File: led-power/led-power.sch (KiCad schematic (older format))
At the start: 70 parts, among them J1 String1, J10 PowerInput, J2 String2, J3 String3, J4 String4, J5 String5, J6 String6, J7 String7, J8 String8, J9 PowerInput, Q1 Q_NMOS_GDS, Q2 Q_NMOS_GDS, Q3 Q_NMOS_GDS, Q4 Q_NMOS_GDS, Q5 Q_NMOS_GDS, Q6 Q_NMOS_GDS, Q7 Q_NMOS_GDS, Q8 Q_NMOS_GDS, U1 MCP6V51, U10 L78L05ACZ-AP, U11 MCP1501, U2 MCP6V51, U3 MCP6V51, U4 MCP6V51, U5 MCP6V51, U6 MCP6V51, U7 MCP6V51, U8 MCP6V51

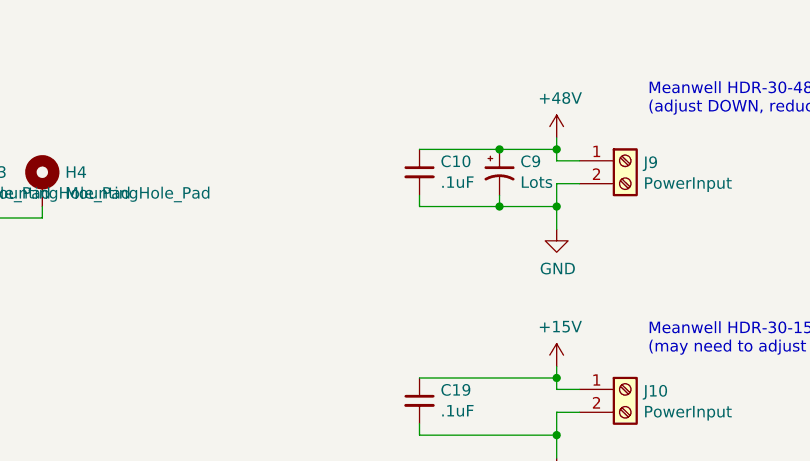
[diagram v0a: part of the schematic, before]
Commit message: Lots of LED power bring-up corrections
* MSOP-8 footprint for op amps
* TO-220 footprint for FETs
* Moved C10 away from J9
* Stopped bothering with length-adjusted traces to resistors
* Moved diodes away from LED strip terminals
* Silkscreen tweaks
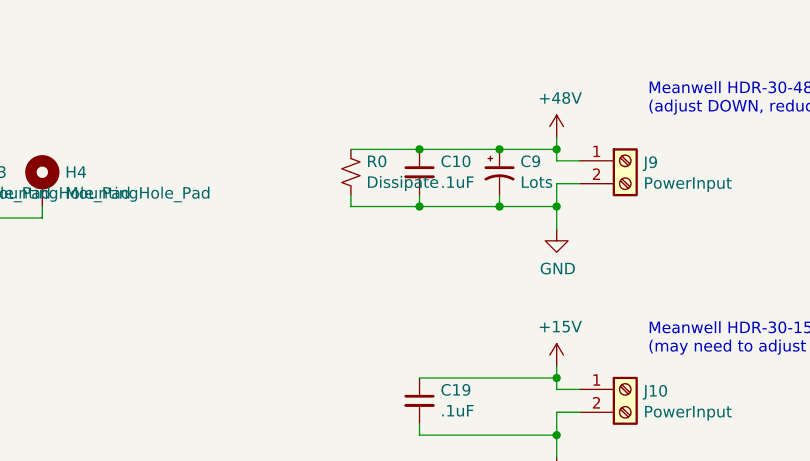
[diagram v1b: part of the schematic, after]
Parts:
- added R0: Dissipate, Resistors_SMD:R_0805_HandSoldering, symbol Device:R_Small_US
- Q1, Q2, Q3, Q4, Q5, Q6, Q7, Q8: footprint TO_SOT_Packages_THT:SIPAK_Vertical -> TO_SOT_Packages_THT:TO-220-3_Vertical
- U1, U2, U3, U4, U5, U6, U7, U8: footprint SMD_Packages:SOIC-8-N -> Housings_SSOP:MSOP-8_3x3mm_Pitch0.65mm
- U10: footprint TO_SOT_Packages_THT:TO-92_Inline_Narrow_Oval -> TO_SOT_Packages_THT:TO-92_Inline_Wide
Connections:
- net +48V: now also R0.1
- net GND: now also R0.2
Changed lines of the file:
@@
 F 0 "Q1" H 2404 1596 50  0000 L CNN
 F 1 "Q_NMOS_GDS" H 2404 1505 50  0000 L CNN
-F 2 "TO_SOT_Packages_THT:SIPAK_Vertical" H 2400 1650 50  0001 C CNN
+F 2 "TO_SOT_Packages_THT:TO-220-3_Vertical" H 2400 1650 50  0001 C CNN
 F 3 "~" H 2200 1550 50  0001 C CNN
 	1    2200 1550
@@
 F 0 "U1" H 1550 1900 50  0000 L CNN
 F 1 "MCP6V51" H 1550 1800 50  0000 L CNN
-F 2 "SMD_Packages:SOIC-8-N" H 1450 1350 50  0001 L CNN
+F 2 "Housings_SSOP:MSOP-8_3x3mm_Pitch0.65mm" H 1450 1350 50  0001 L CNN
 F 3 "http://www.ti.com/lit/ds/symlink/lm6171.pdf" H 1700 1700 50  0001 C CNN
 	1    1550 1550
@@
 F 0 "U10" H 14450 2242 50  0000 C CNN
 F 1 "L78L05ACZ-AP" H 14450 2151 50  0000 C CNN
-F 2 "TO_SOT_Packages_THT:TO-92_Inline_Narrow_Oval" H 14450 2225 50  0001 C CIN
+F 2 "TO_SOT_Packages_THT:TO-92_Inline_Wide" H 14450 2225 50  0001 C CIN
 F 3 "https://www.onsemi.cn/PowerSolutions/document/MC7800-D.PDF" H 14450 1950 50  0001 C CNN
 	1    14450 2000
@@
 F 0 "Q2" H 2404 3346 50  0000 L CNN
 F 1 "Q_NMOS_GDS" H 2404 3255 50  0000 L CNN
-F 2 "TO_SOT_Packages_THT:SIPAK_Vertical" H 2400 3400 50  0001 C CNN
+F 2 "TO_SOT_Packages_THT:TO-220-3_Vertical" H 2400 3400 50  0001 C CNN
 F 3 "~" H 2200 3300 50  0001 C CNN
 	1    2200 3300
@@
 F 0 "U2" H 1550 3650 50  0000 L CNN
 F 1 "MCP6V51" H 1550 3550 50  0000 L CNN
-F 2 "SMD_Packages:SOIC-8-N" H 1450 3100 50  0001 L CNN
+F 2 "Housings_SSOP:MSOP-8_3x3mm_Pitch0.65mm" H 1450 3100 50  0001 L CNN
 F 3 "http://www.ti.com/lit/ds/symlink/lm6171.pdf" H 1700 3450 50  0001 C CNN
 	1    1550 3300
@@
 F 0 "Q3" H 2404 5096 50  0000 L CNN
 F 1 "Q_NMOS_GDS" H 2404 5005 50  0000 L CNN
-F 2 "TO_SOT_Packages_THT:SIPAK_Vertical" H 2400 5150 50  0001 C CNN
+F 2 "TO_SOT_Packages_THT:TO-220-3_Vertical" H 2400 5150 50  0001 C CNN
 F 3 "~" H 2200 5050 50  0001 C CNN
 	1    2200 5050
@@
 F 0 "U3" H 1550 5400 50  0000 L CNN
 F 1 "MCP6V51" H 1550 5300 50  0000 L CNN
-F 2 "SMD_Packages:SOIC-8-N" H 1450 4850 50  0001 L CNN
+F 2 "Housings_SSOP:MSOP-8_3x3mm_Pitch0.65mm" H 1450 4850 50  0001 L CNN
 F 3 "http://www.ti.com/lit/ds/symlink/lm6171.pdf" H 1700 5200 50  0001 C CNN
 	1    1550 5050
@@
 F 0 "Q4" H 2404 6846 50  0000 L CNN
 F 1 "Q_NMOS_GDS" H 2404 6755 50  0000 L CNN
-F 2 "TO_SOT_Packages_THT:SIPAK_Vertical" H 2400 6900 50  0001 C CNN
+F 2 "TO_SOT_Packages_THT:TO-220-3_Vertical" H 2400 6900 50  0001 C CNN
 F 3 "~" H 2200 6800 50  0001 C CNN
 	1    2200 6800
@@
 F 0 "U4" H 1550 7150 50  0000 L CNN
 F 1 "MCP6V51" H 1550 7050 50  0000 L CNN
-F 2 "SMD_Packages:SOIC-8-N" H 1450 6600 50  0001 L CNN
+F 2 "Housings_SSOP:MSOP-8_3x3mm_Pitch0.65mm" H 1450 6600 50  0001 L CNN
 F 3 "http://www.ti.com/lit/ds/symlink/lm6171.pdf" H 1700 6950 50  0001 C CNN
 	1    1550 6800
@@
 F 0 "Q5" H 5204 1596 50  0000 L CNN
 F 1 "Q_NMOS_GDS" H 5204 1505 50  0000 L CNN
-F 2 "TO_SOT_Packages_THT:SIPAK_Vertical" H 5200 1650 50  0001 C CNN
+F 2 "TO_SOT_Packages_THT:TO-220-3_Vertical" H 5200 1650 50  0001 C CNN
 F 3 "~" H 5000 1550 50  0001 C CNN
 	1    5000 1550
@@
 F 0 "U5" H 4350 1900 50  0000 L CNN
 F 1 "MCP6V51" H 4350 1800 50  0000 L CNN
-F 2 "SMD_Packages:SOIC-8-N" H 4250 1350 50  0001 L CNN
+F 2 "Housings_SSOP:MSOP-8_3x3mm_Pitch0.65mm" H 4250 1350 50  0001 L CNN
 F 3 "http://www.ti.com/lit/ds/symlink/lm6171.pdf" H 4500 1700 50  0001 C CNN
 	1    4350 1550
@@
 F 0 "Q6" H 5204 3296 50  0000 L CNN
 F 1 "Q_NMOS_GDS" H 5204 3205 50  0000 L CNN
-F 2 "TO_SOT_Packages_THT:SIPAK_Vertical" H 5200 3350 50  0001 C CNN
+F 2 "TO_SOT_Packages_THT:TO-220-3_Vertical" H 5200 3350 50  0001 C CNN
 F 3 "~" H 5000 3250 50  0001 C CNN
 	1    5000 3250
@@
 F 0 "U6" H 4350 3600 50  0000 L CNN
 F 1 "MCP6V51" H 4350 3500 50  0000 L CNN
-F 2 "SMD_Packages:SOIC-8-N" H 4250 3050 50  0001 L CNN
+F 2 "Housings_SSOP:MSOP-8_3x3mm_Pitch0.65mm" H 4250 3050 50  0001 L CNN
 F 3 "http://www.ti.com/lit/ds/symlink/lm6171.pdf" H 4500 3400 50  0001 C CNN
 	1    4350 3250
@@
 F 0 "Q7" H 5204 5096 50  0000 L CNN
 F 1 "Q_NMOS_GDS" H 5204 5005 50  0000 L CNN
-F 2 "TO_SOT_Packages_THT:SIPAK_Vertical" H 5200 5150 50  0001 C CNN
+F 2 "TO_SOT_Packages_THT:TO-220-3_Vertical" H 5200 5150 50  0001 C CNN
 F 3 "~" H 5000 5050 50  0001 C CNN
 	1    5000 5050
@@
 F 0 "U7" H 4350 5400 50  0000 L CNN
 F 1 "MCP6V51" H 4350 5300 50  0000 L CNN
-F 2 "SMD_Packages:SOIC-8-N" H 4250 4850 50  0001 L CNN
+F 2 "Housings_SSOP:MSOP-8_3x3mm_Pitch0.65mm" H 4250 4850 50  0001 L CNN
 F 3 "http://www.ti.com/lit/ds/symlink/lm6171.pdf" H 4500 5200 50  0001 C CNN
 	1    4350 5050
@@
 F 0 "Q8" H 5204 6796 50  0000 L CNN
 F 1 "Q_NMOS_GDS" H 5204 6705 50  0000 L CNN
-F 2 "TO_SOT_Packages_THT:SIPAK_Vertical" H 5200 6850 50  0001 C CNN
+F 2 "TO_SOT_Packages_THT:TO-220-3_Vertical" H 5200 6850 50  0001 C CNN
 F 3 "~" H 5000 6750 50  0001 C CNN
 	1    5000 6750
@@
 F 0 "U8" H 4350 7100 50  0000 L CNN
 F 1 "MCP6V51" H 4350 7000 50  0000 L CNN
-F 2 "SMD_Packages:SOIC-8-N" H 4250 6550 50  0001 L CNN
+F 2 "Housings_SSOP:MSOP-8_3x3mm_Pitch0.65mm" H 4250 6550 50  0001 L CNN
 F 3 "http://www.ti.com/lit/ds/symlink/lm6171.pdf" H 4500 6900 50  0001 C CNN
 	1    4350 6750
@@
 Wire Wire Line
 	14850 2000 15000 2000
+$Comp
+L Device:R_Small_US R0
+U 1 1 5FE12C48
+P 9800 1300
+F 0 "R0" H 9868 1346 50  0000 L CNN
+F 1 "Dissipate" H 9868 1255 50  0000 L CNN
+F 2 "Resistors_SMD:R_0805_HandSoldering" H 9800 1300 50  0001 C CNN
+F 3 "~" H 9800 1300 50  0001 C CNN
+	1    9800 1300
+	1    0    0    -1
+$EndComp
+Wire Wire Line
+	10100 1200 9800 1200
+Connection ~ 10100 1200
+Wire Wire Line
+	9800 1400 9800 1450
+Wire Wire Line
+	9800 1450 10100 1450
+Connection ~ 10100 1450
 $EndSCHEMATC

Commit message: Reverse polarity diodes; Qwiic header&IO Expander
Also includes relevant connections for the IO expander to the
feedback nets, and /SHDN on the voltage reference.
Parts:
- added C21: 4.7uF, Capacitors_SMD:C_0805_HandSoldering, symbol Device:C_Small
- added C22: 0.1uF, Capacitors_SMD:C_0805_HandSoldering, symbol Device:C_Small
- added C23: 300pF, Capacitors_SMD:C_0805_HandSoldering, symbol Device:C_Small
- added D10, D9: D_Small_ALT, Diodes_SMD:D_SOD-123F, symbol Device:D_Small_ALT
- added J11: Qwiic, Connectors_JST:JST_SH_SM04B-SRSS-TB_04x1.00mm_Angled, symbol Connector:Conn_01x04_Female
- added R11, R12, R13, R14, R15, R16, R17, R18: 43k, Resistors_SMD:R_0805_HandSoldering, symbol Device:R_Small_US
- added R9: 3600, Resistors_SMD:R_0805_HandSoldering, symbol Device:R_Small_US
- added U9: MCP23017_SO, Housings_SOIC:SOIC-28W_7.5x17.9mm_Pitch1.27mm, symbol Interface_Expansion:MCP23017_SO
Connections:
- net +15V: now also D10.1 (K); no longer J10.1 (Pin_1)
- net +48V: now also D9.1 (K); no longer J9.1 (Pin_1)
- net +5V: now also R9.1; no longer U11.3 (/SHDN)
- net GND: now also C21.2, C22.2, C23.2, J11.1 (Pin_1), U9.10 (VSS), U9.15 (A0), U9.16 (A1), U9.17 (A2)
- net VREF: now also C23.1
- net Feedback1: now reaches Q1.3 (S), R1.1, U1.2 (-)
- net Feedback1: now also R11.1
- net Feedback2: now reaches Q2.3 (S), R2.1, U2.2 (-)
- net Feedback2: now also R12.1
- net Feedback3: now reaches Q3.3 (S), R3.1, U3.2 (-)
- net Feedback3: now also R13.1
- net Feedback4: now reaches Q4.3 (S), R4.1, U4.2 (-)
- net Feedback4: now also R14.1
- net Feedback5: now reaches Q5.3 (S), R5.1, U5.2 (-)
- net Feedback5: now also R15.1
- net Feedback6: now reaches Q6.3 (S), R6.1, U6.2 (-)
- net Feedback6: now also R16.1
- net Feedback7: now reaches Q7.3 (S), R7.1, U7.2 (-)
- net Feedback7: now also R17.1
- net Feedback8: now reaches Q8.3 (S), R8.1, U8.2 (-)
- net Feedback8: now also R18.1
- new net: D9.2 (A), J9.1 (Pin_1)
- new net: D10.2 (A), J10.1 (Pin_1)
- new net: R14.2, U9.21 (GPA0)
- new net: R13.2, U9.22 (GPA1)
- new net: R12.2, U9.23 (GPA2)
- new net: R11.2, U9.24 (GPA3)
- new net: R18.2, U9.25 (GPA4)
- new net: R17.2, U9.26 (GPA5)
- new net: R16.2, U9.27 (GPA6)
- new net: R15.2, U9.28 (GPA7)
- new net +3V3: C21.1, C22.1, J11.2 (Pin_2), U9.18 (~RESET~), U9.9 (VDD)
- new net SCL: J11.4 (Pin_4), U9.12 (SCK)
- new net SDA: J11.3 (Pin_3), U9.13 (SDA)
- new net ~SHDN: R9.2, U11.3 (/SHDN), U9.8 (GPB7)
- no-connect marks 0 -> 9
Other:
- moved on the sheet: J10, J9

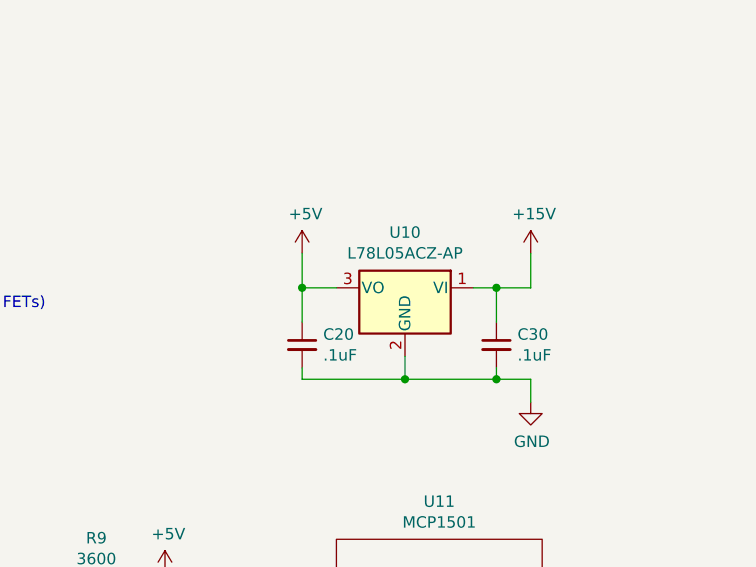
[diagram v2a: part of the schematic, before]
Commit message: Correct 5V regulator orientation and give the GND pin more thermal relief.
Slightly rearranged the traces coming out of the MCP1501.
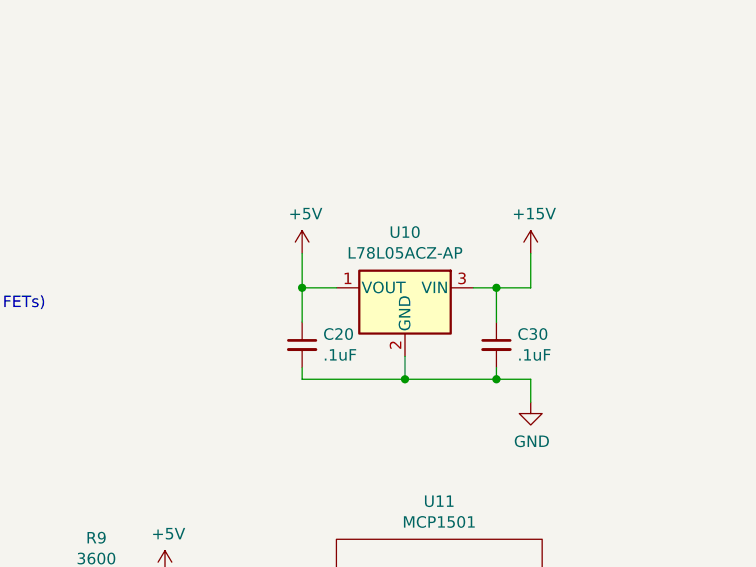
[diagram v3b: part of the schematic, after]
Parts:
- removed U10: L78L05ACZ-AP, TO_SOT_Packages_THT:TO-92_Inline_Wide, symbol Regulator_Linear:LM7805_TO220
- added U10: L78L05ACZ-AP, TO_SOT_Packages_THT:TO-92_Inline_Wide, symbol Regulator_Linear:AP2204RB-3.3
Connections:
- net +15V: now also U10.3 (VIN)
- net +5V: now also U10.1 (VOUT)
- net GND: now also U10.2 (GND)
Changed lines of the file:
@@
 Wire Wire Line
 	10700 1350 10700 1450
-$Comp
-L Regulator_Linear:LM7805_TO220 U10
-U 1 1 5FAD8BDA
-P 14450 2000
-F 0 "U10" H 14450 2242 50  0000 C CNN
-F 1 "L78L05ACZ-AP" H 14450 2151 50  0000 C CNN
-F 2 "TO_SOT_Packages_THT:TO-92_Inline_Wide" H 14450 2225 50  0001 C CIN
-F 3 "https://www.onsemi.cn/PowerSolutions/document/MC7800-D.PDF" H 14450 1950 50  0001 C CNN
-	1    14450 2000
-	-1   0    0    -1
-$EndComp
 Wire Wire Line
 	14150 2000 14000 2000
@@
 NoConn ~ 10500 5750
 NoConn ~ 10500 5650
+$Comp
+L Regulator_Linear:AP2204RB-3.3 U10
+U 1 1 626D114E
+P 14450 2000
+F 0 "U10" H 14450 2242 50  0000 C CNN
+F 1 "L78L05ACZ-AP" H 14450 2151 50  0000 C CNN
+F 2 "TO_SOT_Packages_THT:TO-92_Inline_Wide" H 14450 2225 50  0001 C CNN
+F 3 "https://www.diodes.com/assets/Datasheets/AP2204.pdf" H 14450 2000 50  0001 C CNN
+	1    14450 2000
+	-1   0    0    -1
+$EndComp
 $EndSCHEMATC

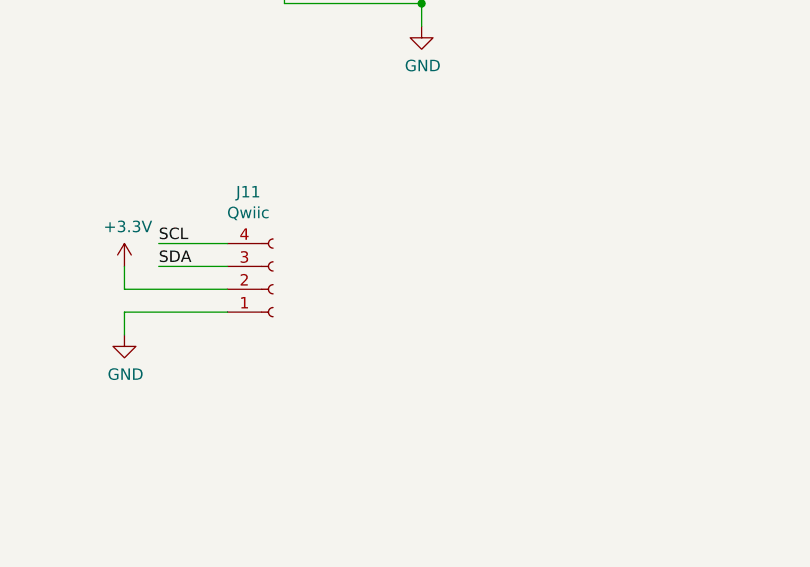
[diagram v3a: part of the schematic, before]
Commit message: Add a second Qwiic header, for chaining
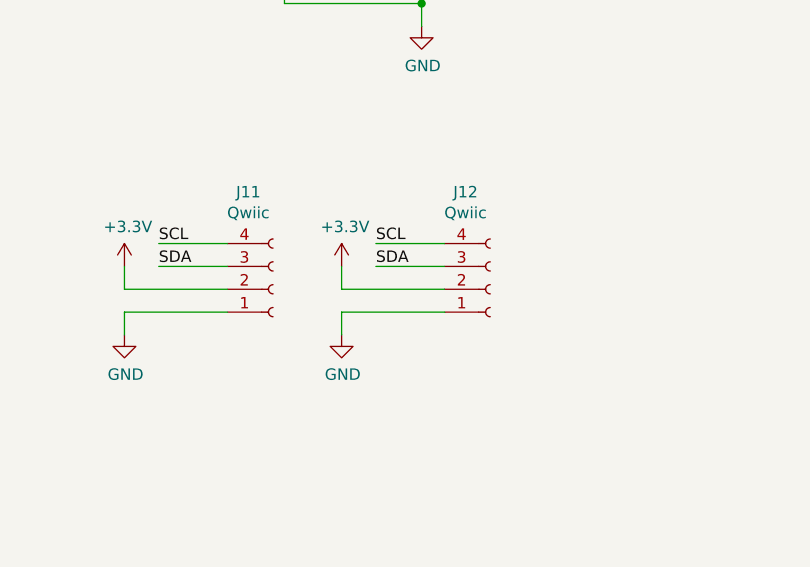
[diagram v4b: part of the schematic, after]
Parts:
- added J12: Qwiic, Connectors_JST:JST_SH_SM04B-SRSS-TB_04x1.00mm_Angled, symbol Connector:Conn_01x04_Female
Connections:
- net +3V3: now also J12.2 (Pin_2)
- net GND: now also J12.1 (Pin_1)
- net SCL: now also J12.4 (Pin_4)
- net SDA: now also J12.3 (Pin_3)
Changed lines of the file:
@@
 	-1   0    0    -1
 $EndComp
+$Comp
+L Connector:Conn_01x04_Female J12
+U 1 1 5FE41F6A
+P 11000 3700
+F 0 "J12" H 10892 3275 50  0000 C CNN
+F 1 "Qwiic" H 10892 3366 50  0000 C CNN
+F 2 "Connectors_JST:JST_SH_SM04B-SRSS-TB_04x1.00mm_Angled" H 11000 3700 50  0001 C CNN
+F 3 "~" H 11000 3700 50  0001 C CNN
+	1    11000 3700
+	1    0    0    1
+$EndComp
+Wire Wire Line
+	10800 3500 10500 3500
+Wire Wire Line
+	10800 3600 10500 3600
+Wire Wire Line
+	10800 3700 10350 3700
+Text Label 10500 3500 0    50   ~ 0
+SCL
+Text Label 10500 3600 0    50   ~ 0
+SDA
+Wire Wire Line
+	10350 3700 10350 3600
+$Comp
+L power:+3.3V #PWR0140
+U 1 1 5FE41F76
+P 10350 3600
+F 0 "#PWR0140" H 10350 3450 50  0001 C CNN
+F 1 "+3.3V" H 10365 3773 50  0000 C CNN
+F 2 "" H 10350 3600 50  0001 C CNN
+F 3 "" H 10350 3600 50  0001 C CNN
+	1    10350 3600
+	1    0    0    -1
+$EndComp
+Wire Wire Line
+	10350 3800 10350 3900
+Wire Wire Line
+	10350 3800 10800 3800
+$Comp
+L power:GND #PWR0141
+U 1 1 5FE41F7E
+P 10350 3900
+F 0 "#PWR0141" H 10350 3650 50  0001 C CNN
+F 1 "GND" H 10355 3727 50  0000 C CNN
+F 2 "" H 10350 3900 50  0001 C CNN
+F 3 "" H 10350 3900 50  0001 C CNN
+	1    10350 3900
+	1    0    0    -1
+$EndComp
 $EndSCHEMATC

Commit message: Made I2C address configurable to match other boards, tweaked silkscreen
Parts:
- added J13: A0, Pin_Headers:Pin_Header_Straight_1x03_Pitch2.54mm, symbol Connector:Conn_01x03_Male
- added J14: A1, Pin_Headers:Pin_Header_Straight_1x03_Pitch2.54mm, symbol Connector:Conn_01x03_Male
- added J15: A2, Pin_Headers:Pin_Header_Straight_1x03_Pitch2.54mm, symbol Connector:Conn_01x03_Male
- added R10, R19, R20, R21, R22, R23: DNP, Resistors_SMD:R_0805_HandSoldering, symbol Device:R_Small_US
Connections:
- net +3V3: now also J13.3 (Pin_3), J14.3 (Pin_3), J15.3 (Pin_3), R10.1, R20.1, R22.1
- net GND: now also J13.1 (Pin_1), J14.1 (Pin_1), J15.1 (Pin_1), R19.1, R21.1, R23.1; no longer U9.15 (A0), U9.16 (A1), U9.17 (A2)
- new net A0: J13.2 (Pin_2), R10.2, R19.2, U9.15 (A0)
- new net A1: J14.2 (Pin_2), R20.2, R21.2, U9.16 (A1)
- new net A2: J15.2 (Pin_2), R22.2, R23.2, U9.17 (A2)
